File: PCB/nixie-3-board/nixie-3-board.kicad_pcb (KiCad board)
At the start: 2 copper layers, 73.3 x 66.6 mm, 22 parts, among them J1 Conn_01x07_Socket, J2 Conn_01x07_Pin, J3 SFH11-PBPC-D07-ST-BK, J4 SFH11-PBPC-D07-ST-BK, Q1 MPSA42, Q2 MPSA92, U1 74HC595, U2 74141, U3 74141

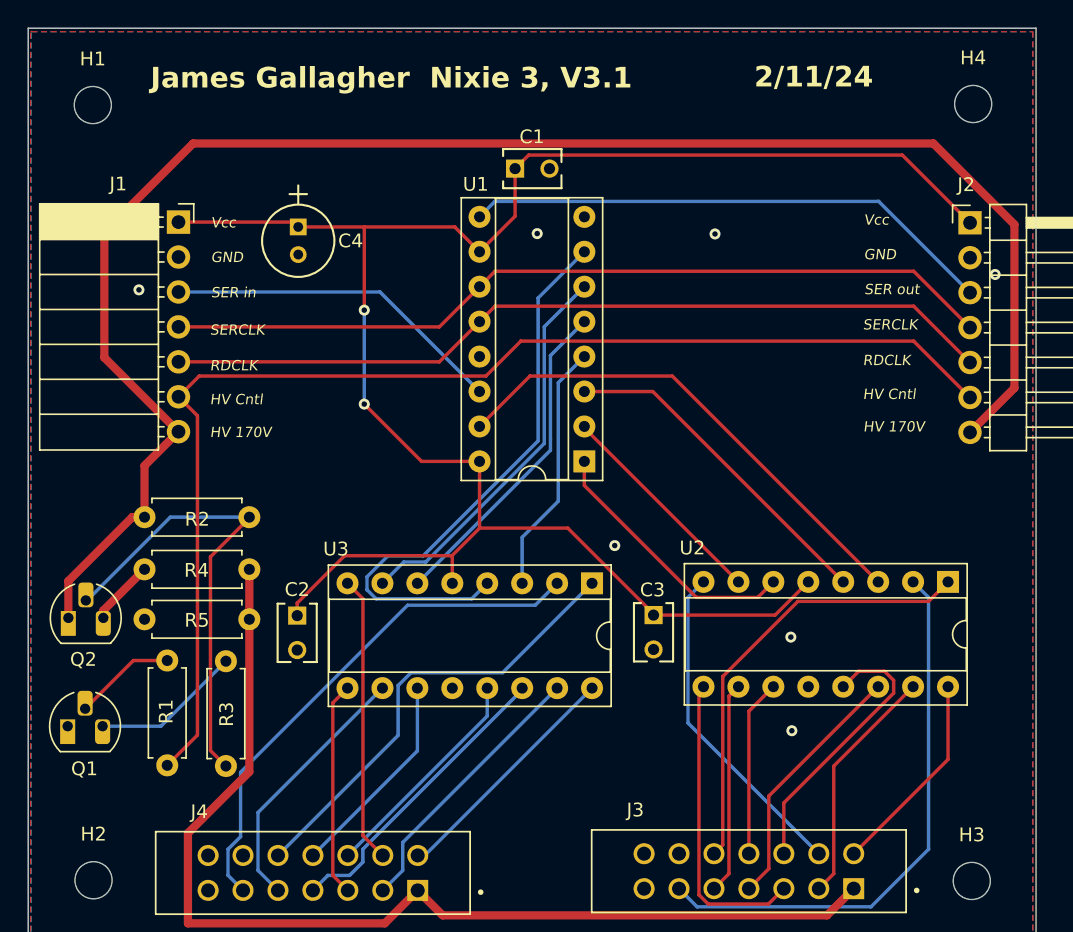
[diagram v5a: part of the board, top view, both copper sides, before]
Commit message: Added high voltage symbol to display PCB
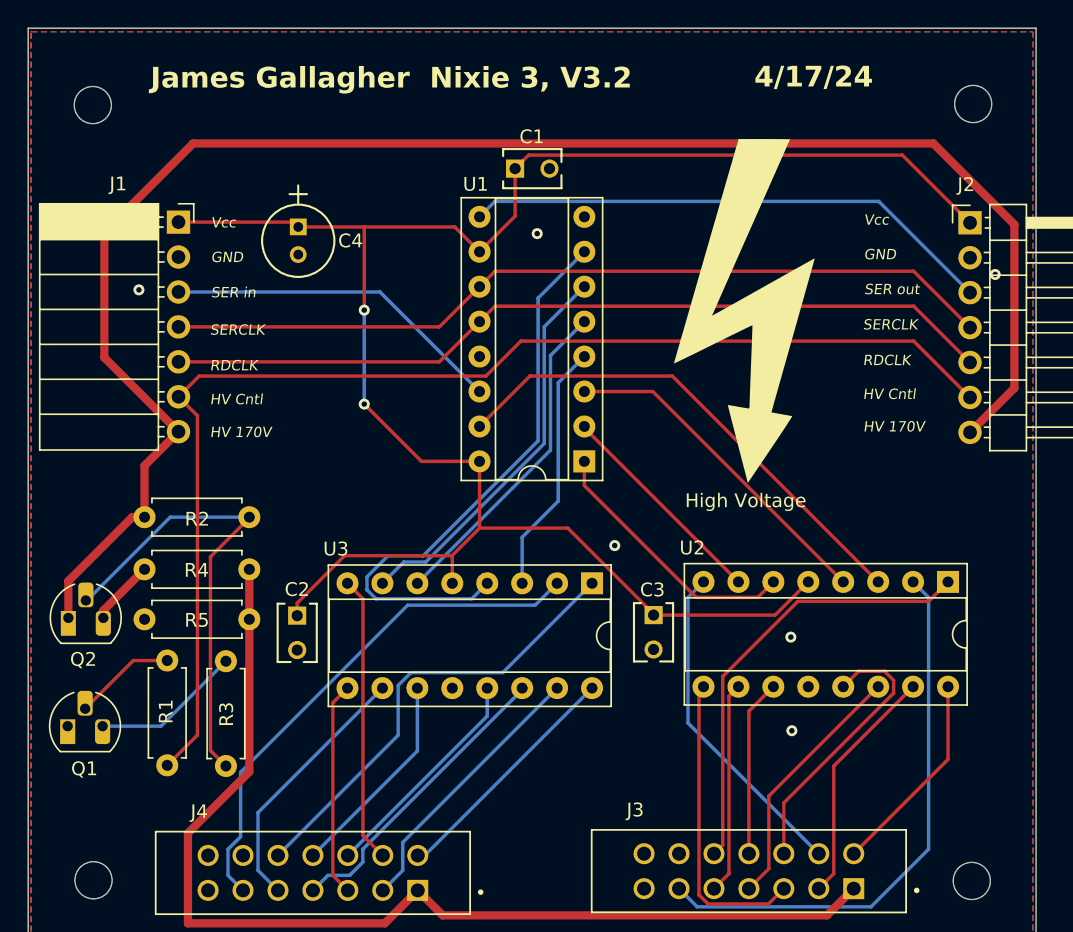
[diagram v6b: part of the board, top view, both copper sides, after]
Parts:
- added G***: LOGO, nixie-3-footprints:High-voltage-25mm-v2-with-text, F.Cu at (97.3, 57.4)
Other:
- board text added: "4/17/24"
- board text added: "James Gallagher Nixie 3, V3.2"
- board text removed: "2/11/24"
- board text removed: "James Gallagher Nixie 3, V3.1"

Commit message: Graphics
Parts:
- added G***: LOGO, nixie-3-footprints:nixie-3-QR, B.Cu at (99.1, 59.7)
- added REF**: OSHW-Logo_5.7x6mm_SilkScreen, Symbol:OSHW-Logo_5.7x6mm_SilkScreen, F.Cu at (70.4, 46.0)
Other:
- board text added: "GitHub"
